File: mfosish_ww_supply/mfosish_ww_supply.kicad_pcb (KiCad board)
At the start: 2 copper layers, 100 x 61 mm, 30 parts, among them J1 Conn_01x02, J2 Conn_01x03, U1 LM7812_TO220, U2 LM7912_TO220

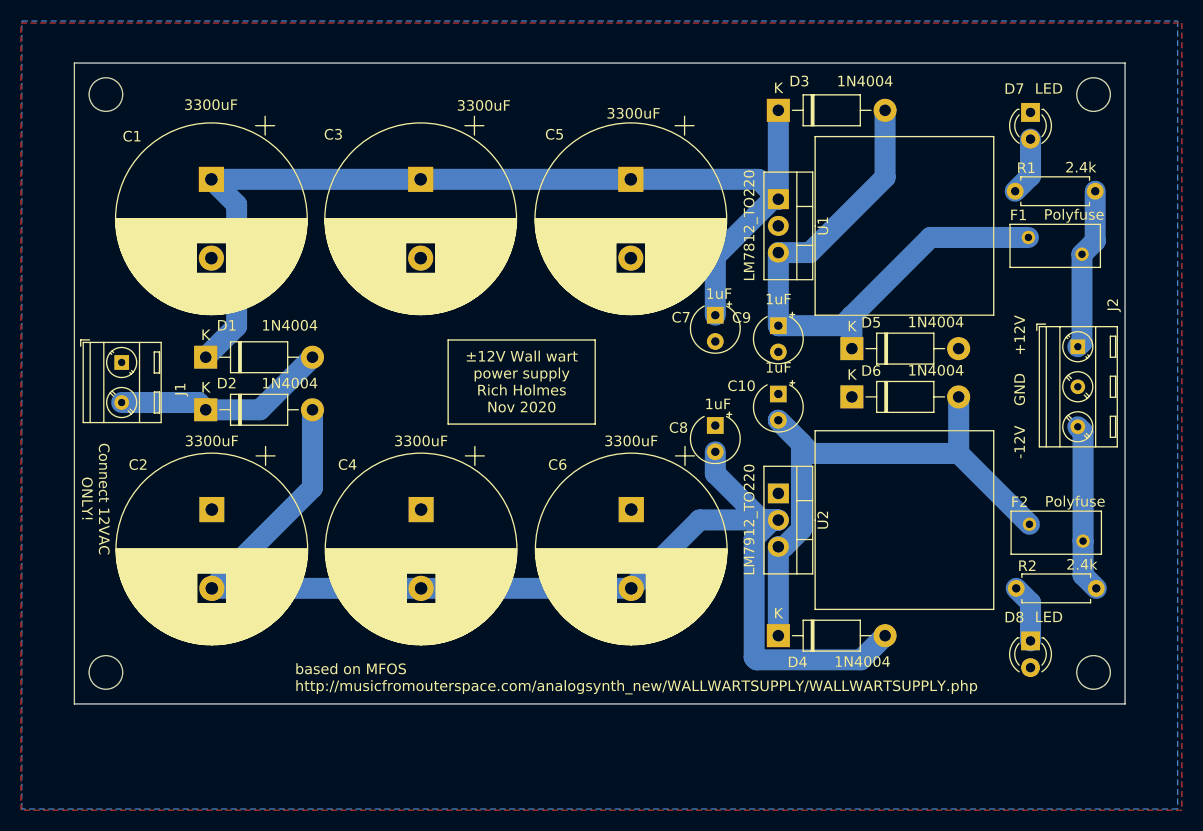
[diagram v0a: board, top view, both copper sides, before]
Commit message: Switch connectors...add text
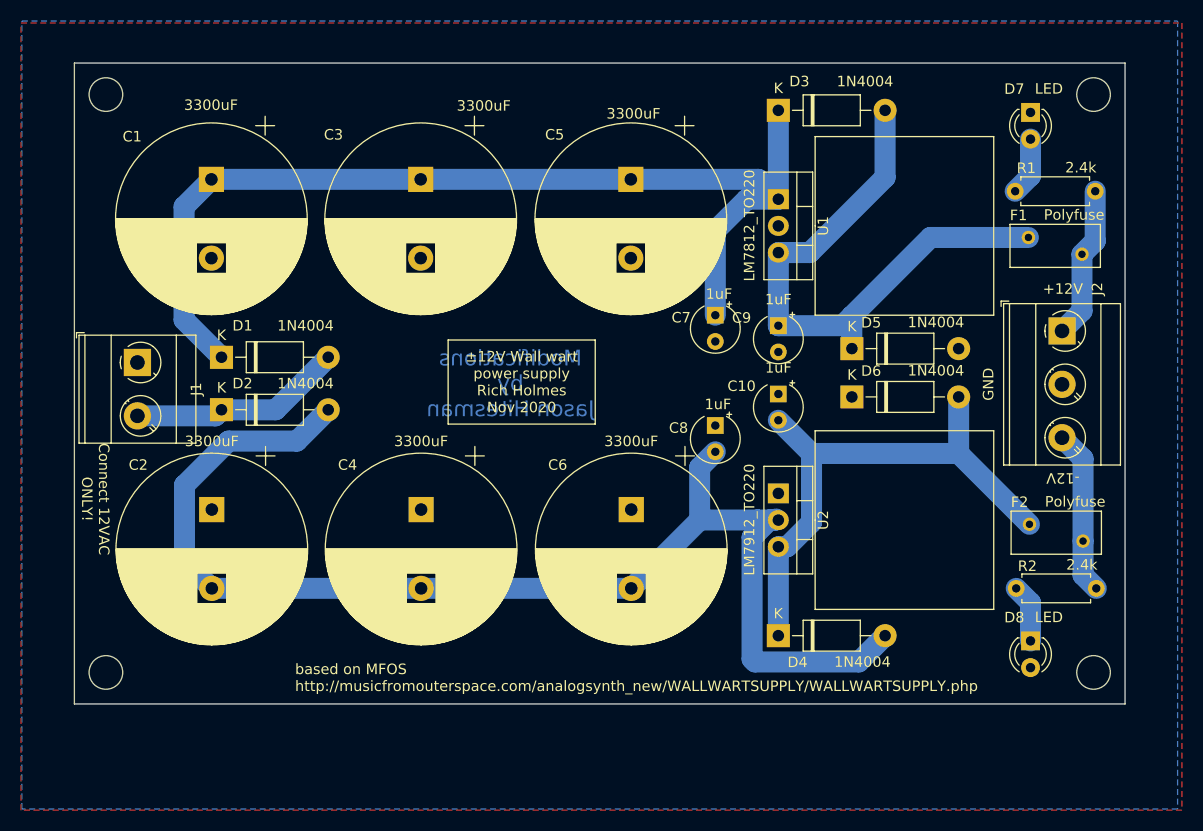
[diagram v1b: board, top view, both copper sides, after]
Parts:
- J1: footprint TerminalBlock_MetzConnect:TerminalBlock_MetzConnect_Type086_RT03402HBLC_1x02_P3.81mm_Horizontal -> TerminalBlock_MetzConnect:TerminalBlock_MetzConnect_Type073_RT02602HBLU_1x02_P5.08mm_Horizontal
- J2: footprint TerminalBlock_MetzConnect:TerminalBlock_MetzConnect_Type086_RT03403HBLC_1x03_P3.81mm_Horizontal -> TerminalBlock_MetzConnect:TerminalBlock_MetzConnect_Type073_RT02603HBLU_1x03_P5.08mm_Horizontal
- moved J2 2.12 mm to (144.0, 89.5)
- moved D1 1.50 mm to (64.0, 92.0)
- moved D2 1.50 mm to (64.0, 97.0)
- moved J1 1.50 mm to (56.0, 92.5)
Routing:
- net Net-(C2-Pad2): track 115.3 -> 119.4 mm
- net Net-(C10-Pad2): track 56.0 -> 52.5 mm
- net Net-(C1-Pad1): track 96.2 -> 98.0 mm
- net +12V: track 15.5 -> 14.6 mm
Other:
- net class PWR: clearance 0.2 -> 0.4
- board text added: "Modifications by Jason Hitesman"
